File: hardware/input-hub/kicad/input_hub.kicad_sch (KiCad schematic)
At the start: 40 parts, among them J1 ACJMIH, J2 ACJMIH, J3 ACJMIH, J4 ACJMIH, J5 8P8C, J6 BM04B-SRSS-TB_LF__SN_, J7 Conn_01x04, J8 Conn_01x02, P1 S2B-PH-SM4-TB_LF__SN_, U1 102010448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

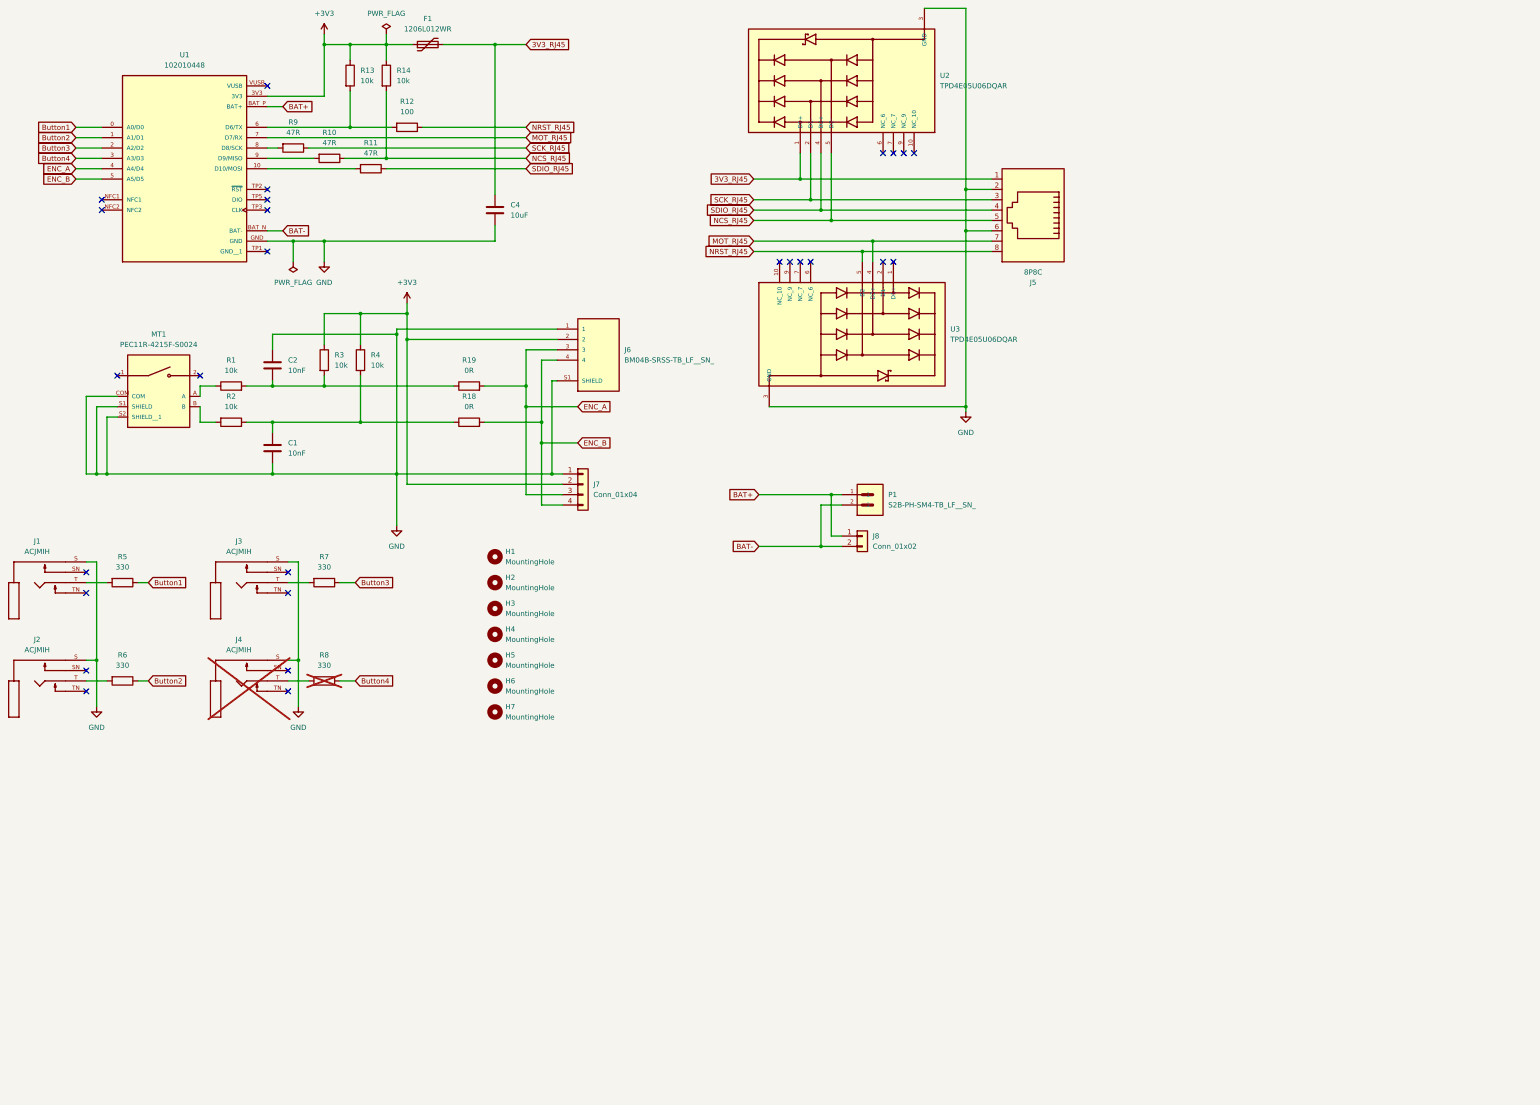
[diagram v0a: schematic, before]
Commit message: fix: refine input hub board draft
Update the input hub KiCad design after
  layout review.

  - Replace solder fallback headers with standard 2.54 mm footprints.
  - Clean up PMW3610 RJ45 routing, ESD placement, and local power conditioning.
  - Add optional SJ1-3523N 3.5 mm jack library assets for future pedal jack variants.
  - Preserve AS5600, EC11, footswitch, battery, and PMW3610 interface options for review.
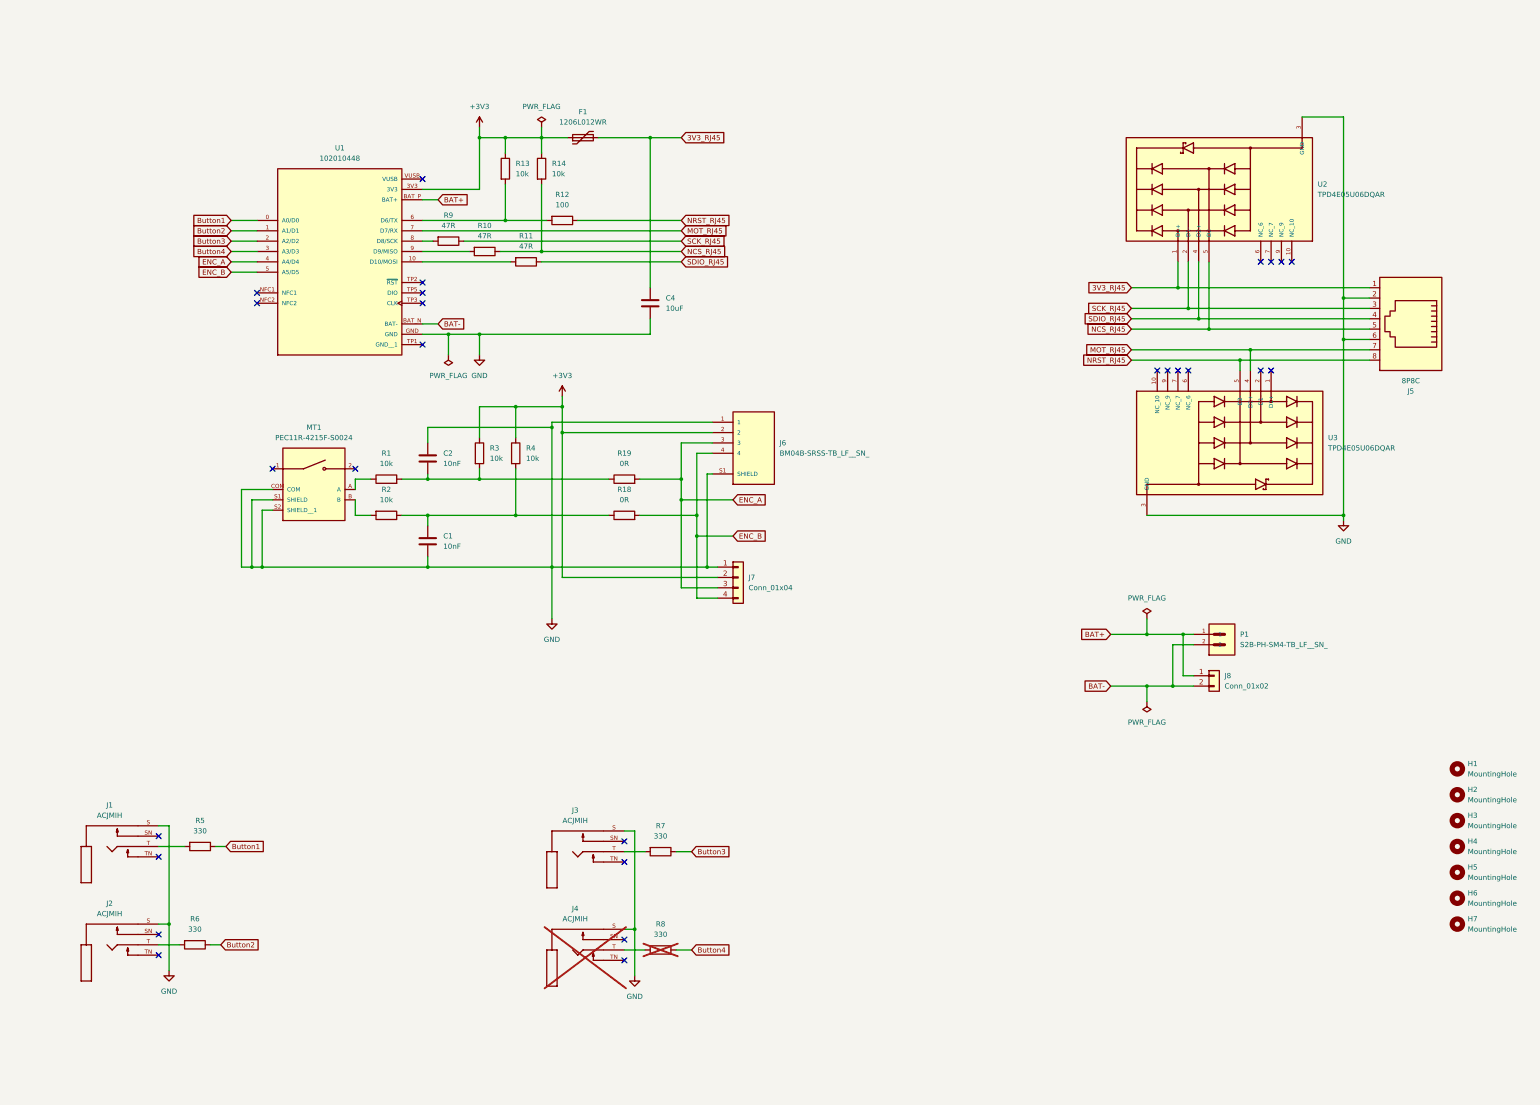
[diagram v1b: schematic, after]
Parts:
- J7: footprint Connector_PinHeader_1.00mm:PinHeader_1x04_P1.00mm_Vertical -> Connector_PinHeader_2.54mm:PinHeader_1x04_P2.54mm_Vertical
- J8: footprint Connector_PinHeader_1.00mm:PinHeader_1x02_P1.00mm_Vertical -> Connector_PinHeader_2.54mm:PinHeader_1x02_P2.54mm_Vertical
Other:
- moved on the sheet: C1, C2, C4, F1, H1, H2, H3, H4, H5, H6, H7, J1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

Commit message: fix: refine input hub battery layout
- Update the battery connector layout.
  - Rename the battery connector from P to J.
  - Add return vias near signal vias.
  - Widen power-path traces.
  - Add XIAO battery solder holes and silkscreen labels.
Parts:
- added J10, J9: Conn_01x01_Pin, Connector_Pin:Pin_D0.7mm_L6.5mm_W1.8mm_FlatFork, symbol Connector:Conn_01x01_Pin
- renumbered P1 to J11
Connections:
- net BAT+: now also J10.1 (Pin_1)
- net BAT-: now also J9.1 (Pin_1)
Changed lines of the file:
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@@
 	)
 	(junction
+		(at 123.19 63.5)
+		(diameter 0)
+		(color 0 0 0 0)
+	)
+	(junction
+		(at 130.81 93.98)
+		(diameter 0)
+		(color 0 0 0 0)
+	)
+	(junction
 		(at 176.53 48.26)
 		(diameter 0)
@@
 	(wire
 		(pts
+			(xy 130.81 93.98) (xy 132.08 93.98)
+		)
+		(stroke
+			(width 0)
+			(type default)
+		)
+	)
+	(wire
+		(pts
 			(xy 187.96 146.05) (xy 196.85 146.05)
 		)
@@
 	(wire
 		(pts
-			(xy 120.65 93.98) (xy 124.46 93.98)
+			(xy 120.65 93.98) (xy 130.81 93.98)
+		)
+		(stroke
+			(width 0)
+			(type default)
+		)
+	)
+	(wire
+		(pts
+			(xy 123.19 52.07) (xy 123.19 63.5)
 		)
 		(stroke
@@
 	(wire
 		(pts
+			(xy 130.81 91.44) (xy 130.81 93.98)
+		)
+		(stroke
+			(width 0)
+			(type default)
+		)
+	)
+	(wire
+		(pts
 			(xy 294.64 100.33) (xy 323.85 100.33)
 		)
@@
 	(wire
 		(pts
+			(xy 123.19 63.5) (xy 132.08 63.5)
+		)
+		(stroke
+			(width 0)
+			(type default)
+		)
+	)
+	(wire
+		(pts
 			(xy 170.18 242.57) (xy 172.72 242.57)
 		)
@@
 	(wire
 		(pts
-			(xy 120.65 63.5) (xy 124.46 63.5)
+			(xy 120.65 63.5) (xy 123.19 63.5)
 		)
 		(stroke
@@
 	(global_label "BAT-"
 		(shape input)
-		(at 124.46 93.98 0)
+		(at 132.08 93.98 0)
 		(fields_autoplaced yes)
 		(effects
@@
 		)
 		(property "Intersheetrefs" "${INTERSHEET_REFS}"
-			(at 132.3438 93.98 0)
+			(at 139.9638 93.98 0)
 			(hide yes)
 			(show_name no)
@@
 	(global_label "BAT+"
 		(shape input)
-		(at 124.46 63.5 0)
+		(at 132.08 63.5 0)
 		(fields_autoplaced yes)
 		(effects
@@
 		)
 		(property "Intersheetrefs" "${INTERSHEET_REFS}"
-			(at 132.3438 63.5 0)
+			(at 139.9638 63.5 0)
 			(hide yes)
 			(show_name no)
@@
 		(dnp no)
 		(fields_autoplaced yes)
-		(property "Reference" "P1"
+		(property "Reference" "J11"
 			(at 321.31 170.1799 0)
 			(show_name no)
@@
 			(project "input_hub"
 				(path "/770eab34-1e0f-45ef-9190-c3b360ed8a79"
-					(reference "P1")
+					(reference "J11")
 					(unit 1)
 				)
@@
 	)
 	(symbol
+		(lib_id "Connector:Conn_01x01_Pin")
+		(at 123.19 46.99 90)
+		(mirror x)
+		(unit 1)
+		(body_style 1)
+		(exclude_from_sim no)
+		(in_bom yes)
+		(on_board yes)
+		(in_pos_files yes)
+		(dnp no)
+		(property "Reference" "J10"
+			(at 121.92 46.3549 90)
+			(show_name no)
+			(do_not_autoplace no)
+			(effects
+				(font
+					(size 1.27 1.27)
+				)
+				(justify left)
+			)
+		)
+		(property "Value" "Conn_01x01_Pin"
+			(at 121.92 48.8949 90)
+			(show_name no)
+			(do_not_autoplace no)
+			(effects
+				(font
+					(size 1.27 1.27)
+				)
+				(justify left)
+			)
+		)
+		(property "Footprint" "Connector_Pin:Pin_D0.7mm_L6.5mm_W1.8mm_FlatFork"
+			(at 123.19 46.99 0)
+			(hide yes)
+			(show_name no)
+			(do_not_autoplace no)
+			(effects
+				(font
+					(size 1.27 1.27)
+				)
+			)
+		)
+		(property "Datasheet" ""
+			(at 123.19 46.99 0)
+			(hide yes)
+			(show_name no)
+			(do_not_autoplace no)
+			(effects
+				(font
+					(size 1.27 1.27)
+				)
+			)
+		)
+		(property "Description" "Generic connector, single row, 01x01, script generated"
+			(at 123.19 46.99 0)
+			(hide yes)
+			(show_name no)
+			(do_not_autoplace no)
+			(effects
+				(font
+					(size 1.27 1.27)
+				)
+			)
+		)
+		(pin "1"
+		)
+		(instances
+			(project "input_hub"
+				(path "/770eab34-1e0f-45ef-9190-c3b360ed8a79"
+					(reference "J10")
+					(unit 1)
+				)
+			)
+		)
+	)
+	(symbol
 		(lib_id "Device:R")
 		(at 64.77 246.38 270)
@@
 					(unit 1)
 				)
+			)
+		)
+	)
+	(symbol
+		(lib_id "Connector:Conn_01x01_Pin")
+		(at 130.81 86.36 270)
+		(unit 1)
+		(body_style 1)
+		(exclude_from_sim no)
+		(in_bom yes)
+		(on_board yes)
+		(in_pos_files yes)
+		(dnp no)
+		(fields_autoplaced yes)
+		(property "Reference" "J9"
+			(at 132.08 85.7249 90)
+			(show_name no)
+			(do_not_autoplace no)
+			(effects
+				(font
+					(size 1.27 1.27)
+				)
+				(justify left)
+			)
+		)
+		(property "Value" "Conn_01x01_Pin"
+			(at 132.08 88.2649 90)
+			(show_name no)
+			(do_not_autoplace no)
+			(effects
+				(font
+					(size 1.27 1.27)
+				)
+				(justify left)
+			)
+		)
+		(property "Footprint" "Connector_Pin:Pin_D0.7mm_L6.5mm_W1.8mm_FlatFork"
+			(at 130.81 86.36 0)
+			(hide yes)
+			(show_name no)
+			(do_not_autoplace no)
+			(effects
+				(font
+					(size 1.27 1.27)
+				)
+			)
+		)
+		(property "Datasheet" ""
+			(at 130.81 86.36 0)
+			(hide yes)
+			(show_name no)
+			(do_not_autoplace no)
+			(effects
+				(font
+					(size 1.27 1.27)
+				)
+			)
+		)
+		(property "Description" "Generic connector, single row, 01x01, script generated"
+			(at 130.81 86.36 0)
+			(hide yes)
+			(show_name no)
+			(do_not_autoplace no)
+			(effects
+				(font
+					(size 1.27 1.27)
+				)
+			)
+		)
+		(pin "1"
+		)
+		(instances
+			(project "input_hub"
+				(path "/770eab34-1e0f-45ef-9190-c3b360ed8a79"
+					(reference "J9")
+					(unit 1)
+				)

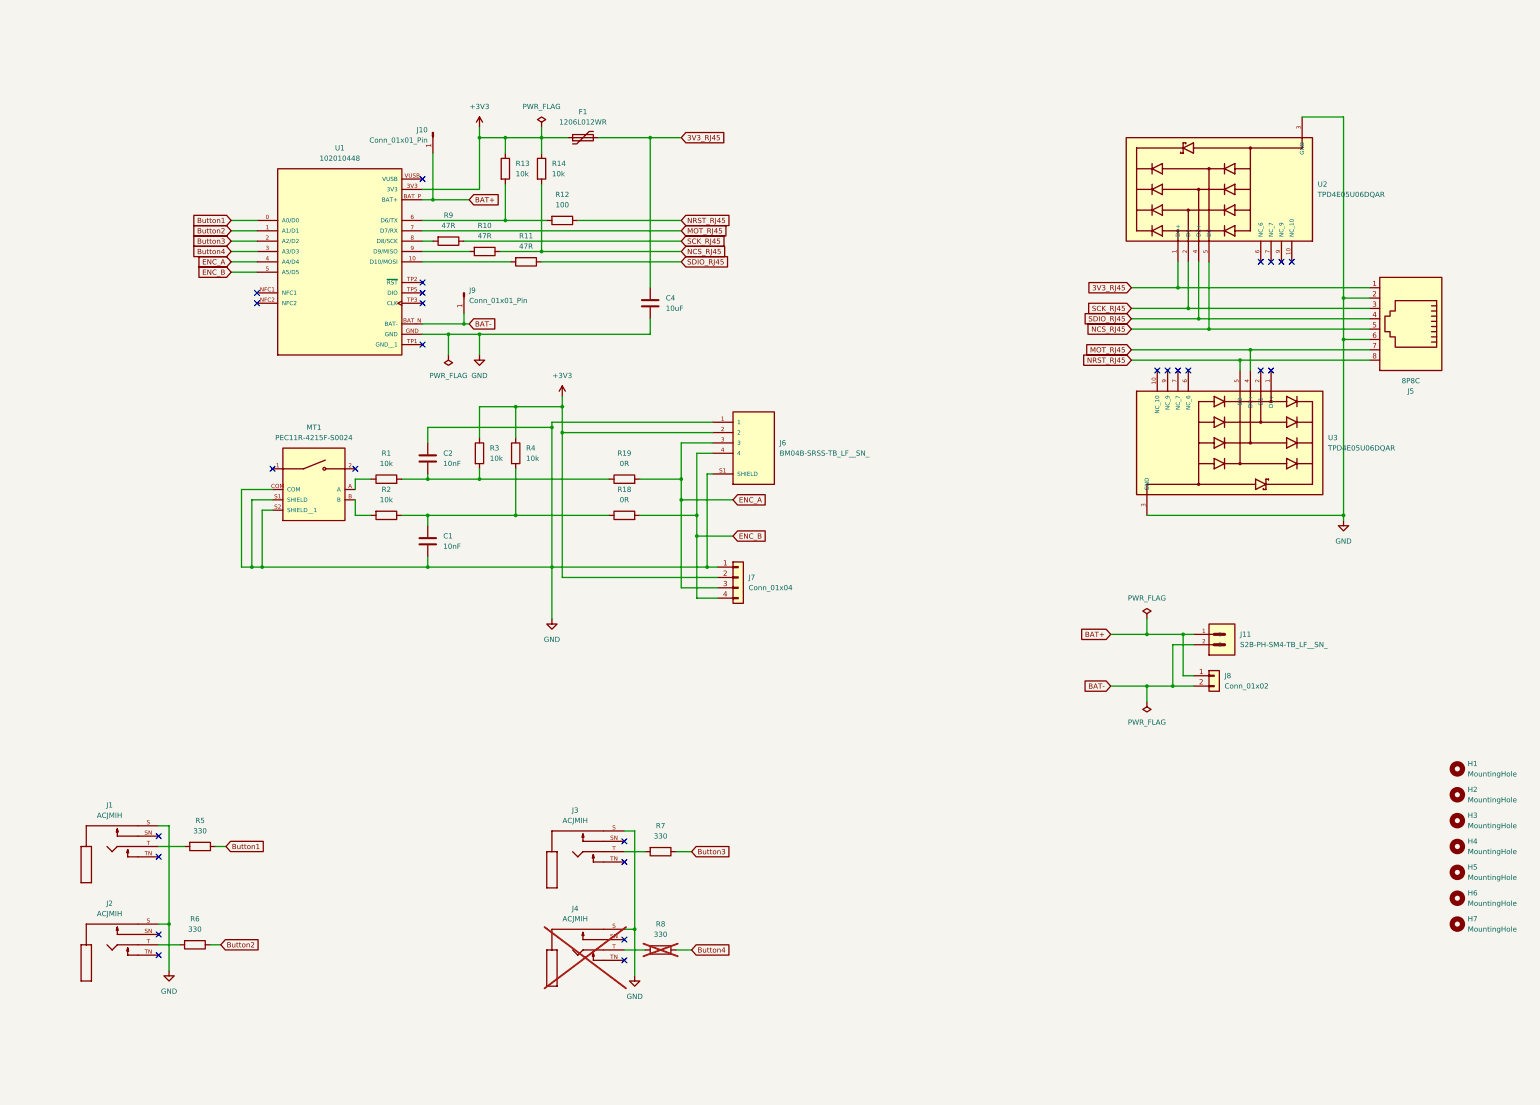
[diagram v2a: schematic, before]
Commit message: fix: make input hub routing more gooder and a schematic change - esd routing and schematic - PEC11R debounce circuit - reduced back side routing - added filter caps to 1/4 inch jacks - made traces thiccer
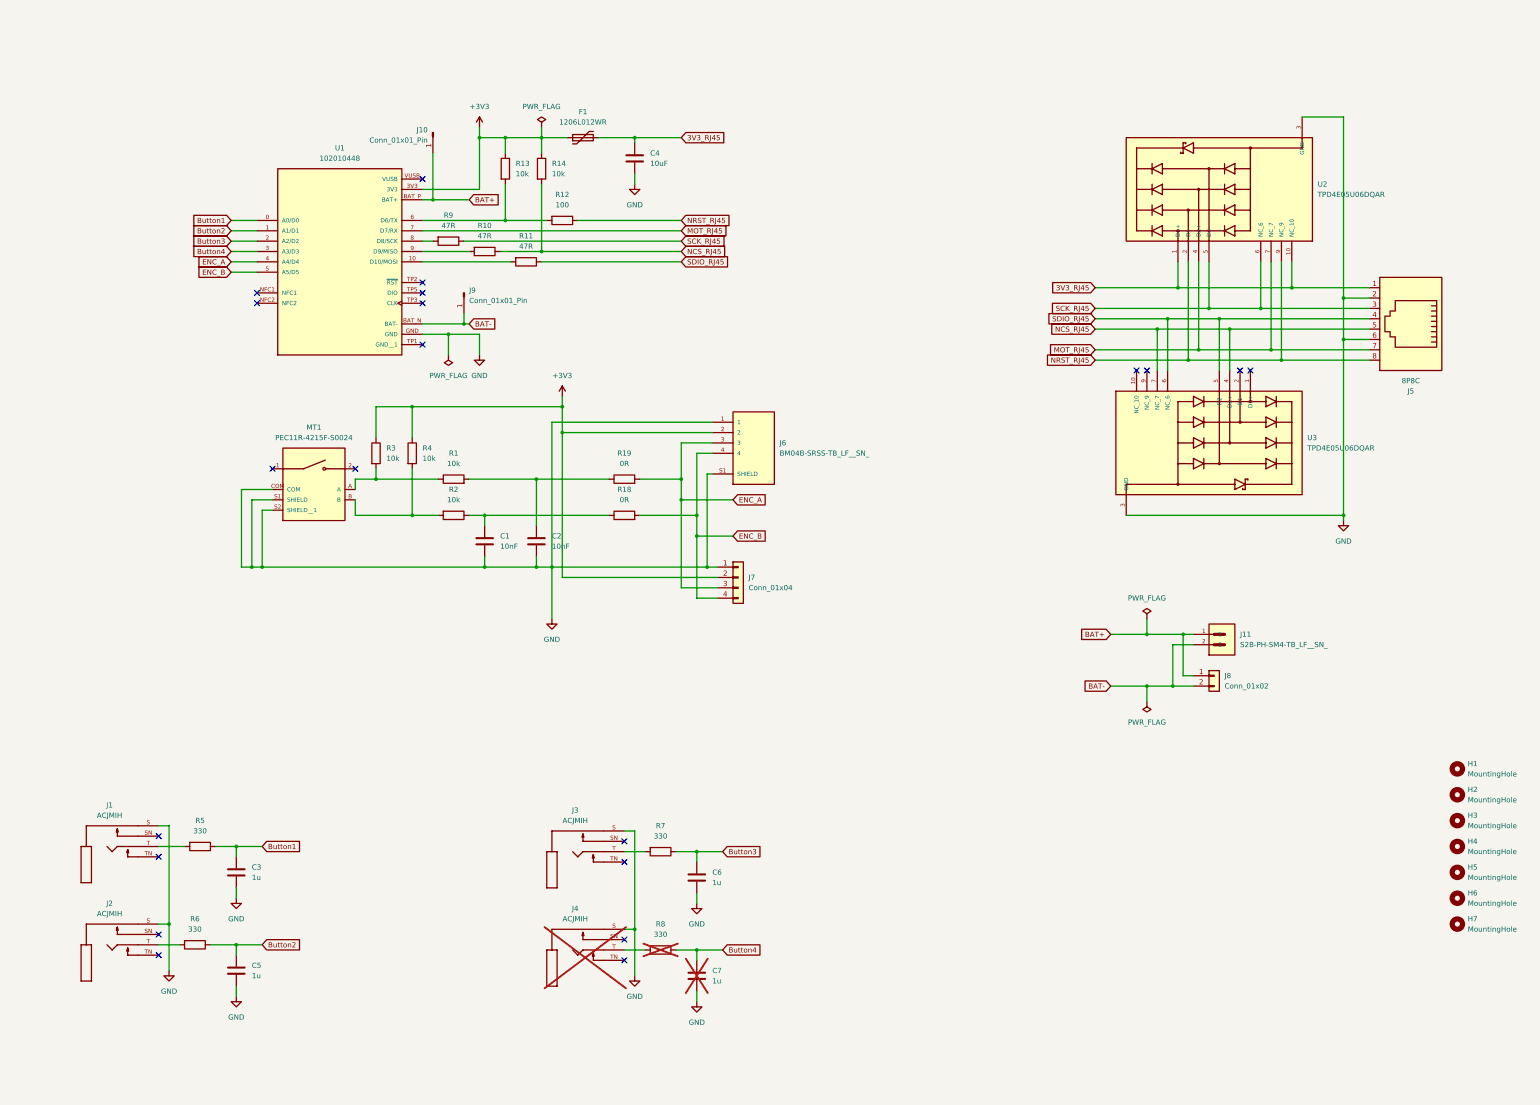
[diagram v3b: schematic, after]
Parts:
- added C3, C5, C6, C7: 1u, Capacitor_SMD:C_0603_1608Metric, symbol Device:C
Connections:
- net 3V3_RJ45: now also U2.10 (NC_10)
- net Button1: now also C3.2
- net Button2: now also C5.2
- net Button3: now also C6.2
- net Button4: now also C7.2
- net GND: now also C3.1, C5.1, C6.1, C7.1
- net MOT_RJ45: now also U2.4 (D2+), U2.7 (NC_7); no longer U3.4 (D2+)
- net NCS_RJ45: now also U3.4 (D2+), U3.7 (NC_7); no longer U2.5 (D2-)
- net NRST_RJ45: now also U2.2 (D1-), U2.9 (NC_9); no longer U3.5 (D2-)
- net SCK_RJ45: now also U2.5 (D2-), U2.6 (NC_6); no longer U2.2 (D1-)
- net SDIO_RJ45: now also U3.5 (D2-), U3.6 (NC_6); no longer U2.4 (D2+)
- net at C1.2, R18.1, R2.1: no longer R4.2
- net at C2.1, R1.2, R19.1: no longer R3.2
- net at MT1.A, R1.1: now also R3.2
- net at MT1.B, R2.2: now also R4.2
- no-connect marks 27 -> 21
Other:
- moved on the sheet: C1, C2, C4, R1, R2, R3, R4, U3
